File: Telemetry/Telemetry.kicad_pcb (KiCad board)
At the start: 2 copper layers, 56.5 x 55 mm, 61 parts, among them J1 Micro_SD_Card, J5 Conn_02x05_Odd_Even, J7 4P4C, J8 4P4C, Q3 Q_NMOS_GSD, SW1 SW_Push, SW3 SW_Push, U3 MAX485E, U4 STM32F103C8Tx, U5 LD1117S50TR_SOT223, U6 MCP1700-3302E_SOT23, Y1 8Mhz

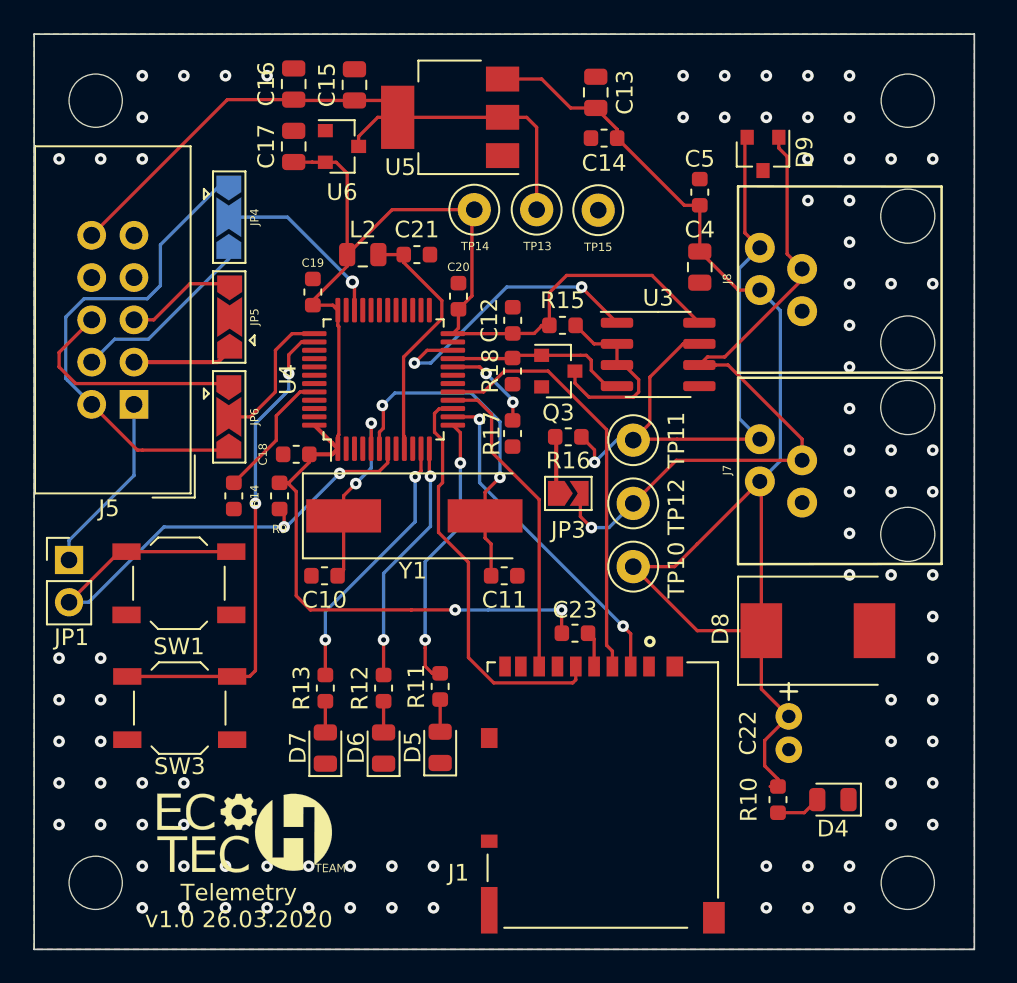
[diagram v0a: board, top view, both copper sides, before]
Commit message: Telemetry/: Gerber fixes
Signed-off-by: Cezarus27 <cs.pol234@gmail.com>
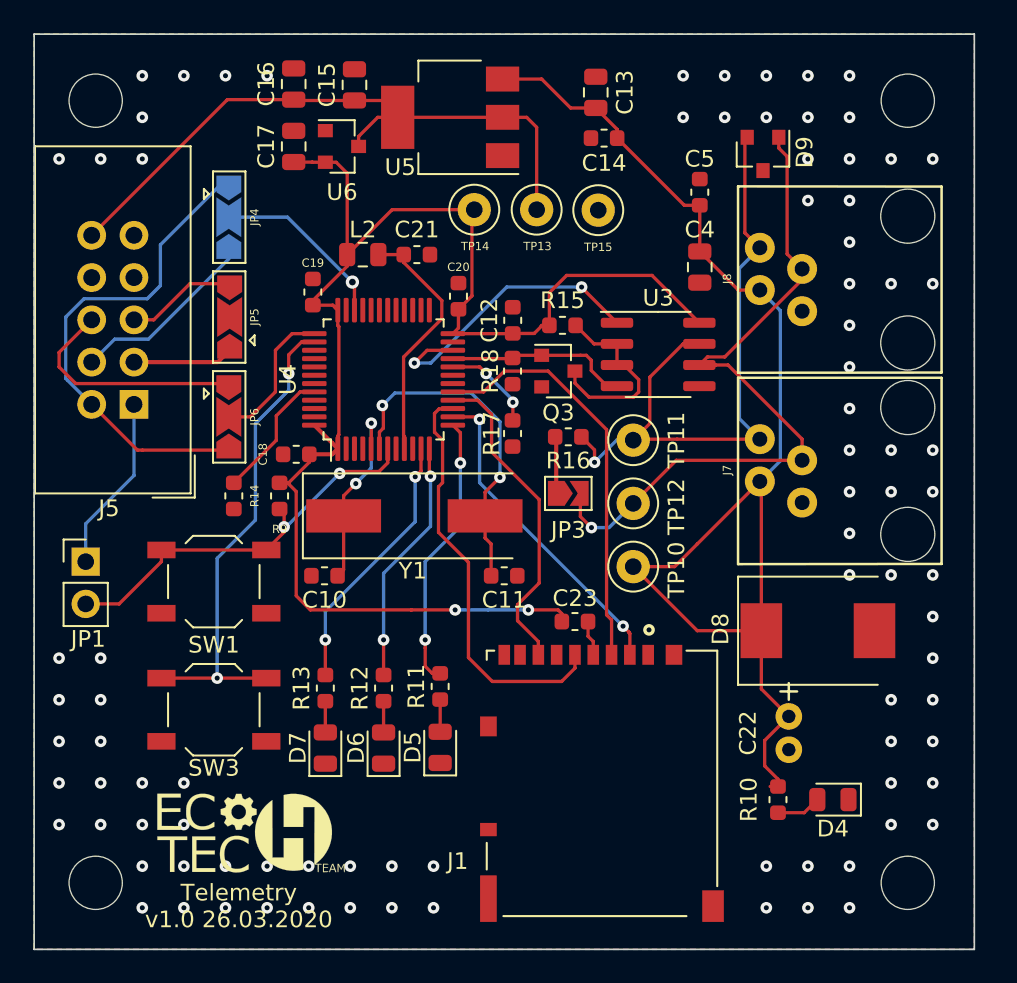
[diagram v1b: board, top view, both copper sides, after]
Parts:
- moved SW1 2.10 mm to (114.3, 132.9)
- moved SW3 2.05 mm to (114.3, 140.6)
- moved JP1 1.00 mm to (106.6, 131.7)
- moved J1 0.70 mm to (137.2, 137.3)
- moved C23 0.70 mm to (136.0, 135.3)
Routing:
- net /RST: track 35.7 -> 24.3 mm
- net +3V3: track 89.2 -> 88.4 mm
- net /MOSI: track 25.6 -> 24.9 mm
- net /CS: track 20.3 -> 19.6 mm

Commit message: Telemetry/: fix PCB size
Signed-off-by: Cezarus27 <cs.pol234@gmail.com>
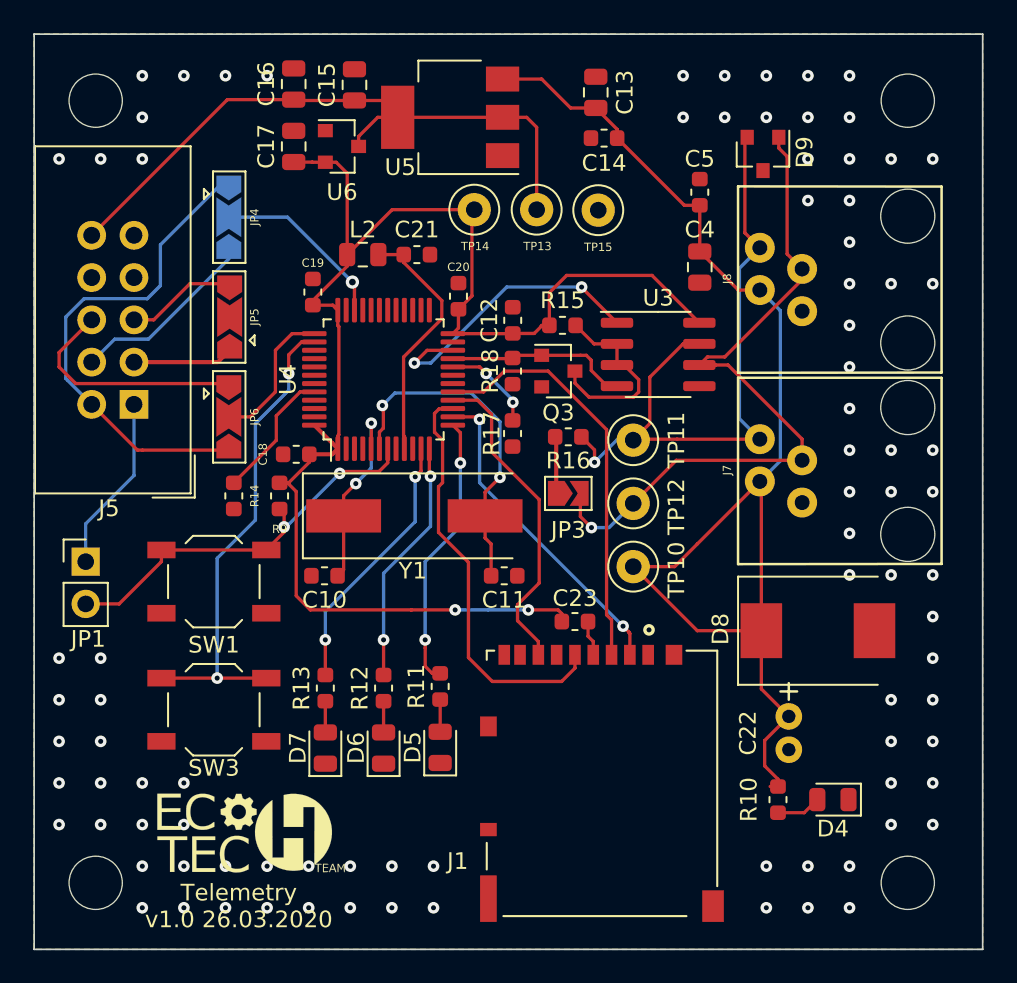
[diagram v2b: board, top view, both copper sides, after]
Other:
- board size 56.5 x 55 mm -> 57 x 55 mm

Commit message: Telemetry/: add test points and rename PCB to v1.3
Signed-off-by: Cezarus27 <cs.pol234@gmail.com>
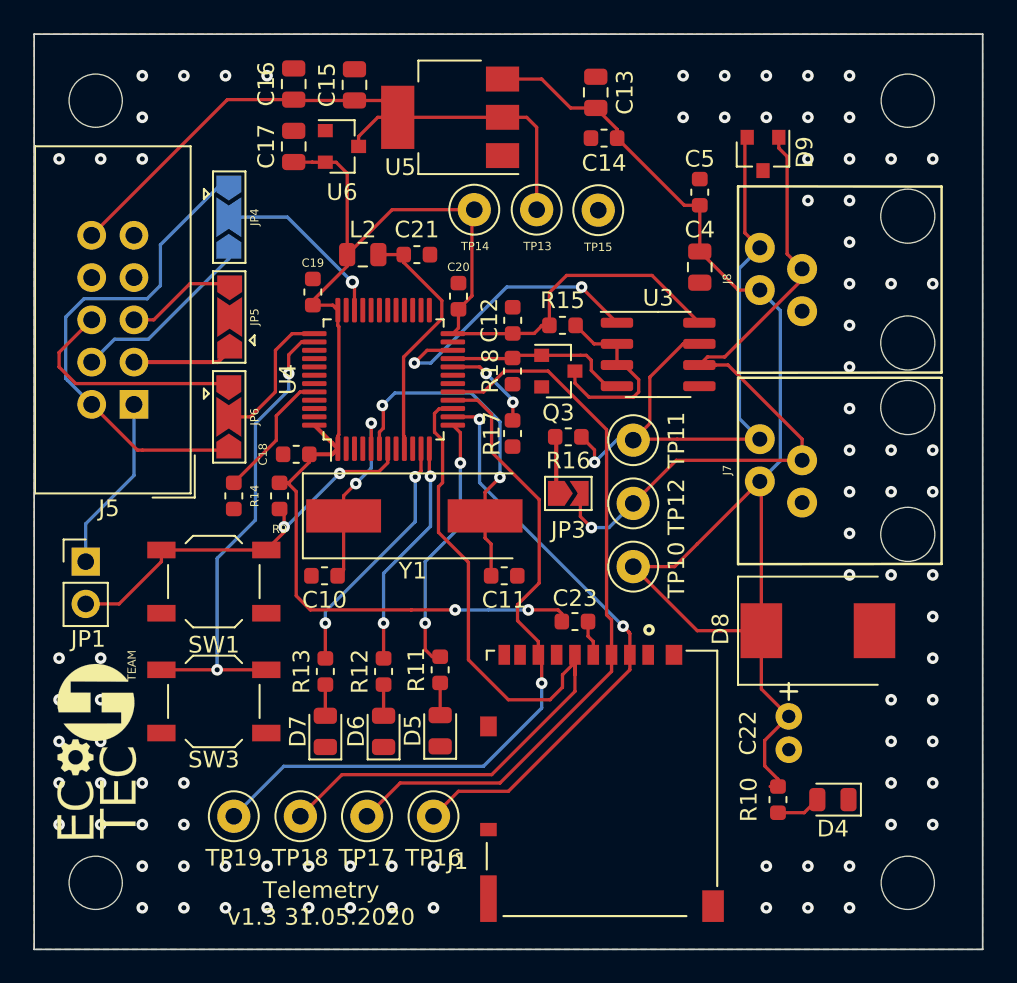
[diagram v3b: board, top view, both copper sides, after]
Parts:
- added TP16: TestPoint, TestPoint:TestPoint_Loop_D1.80mm_Drill1.0mm_Beaded, F.Cu at (127.5, 147.0)
- added TP17: TestPoint, TestPoint:TestPoint_Loop_D1.80mm_Drill1.0mm_Beaded, F.Cu at (123.5, 147.0)
- added TP18: TestPoint, TestPoint:TestPoint_Loop_D1.80mm_Drill1.0mm_Beaded, F.Cu at (119.5, 147.0)
- added TP19: TestPoint, TestPoint:TestPoint_Loop_D1.80mm_Drill1.0mm_Beaded, F.Cu at (115.5, 147.0)
- moved G1 10.2 mm to (107.5, 143.0), turned to 90 degrees
- moved D5 1.00 mm to (127.9, 141.9)
- moved D6 1.00 mm to (124.5, 141.9)
- moved D7 1.00 mm to (121.0, 141.9)
- moved R11 1.00 mm to (127.9, 138.2)
- moved R12 1.00 mm to (124.5, 138.3)
- moved R13 1.00 mm to (121.0, 138.3)
- moved SW3 0.50 mm to (114.3, 140.1)
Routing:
- net /SCK: track 25.1 -> 50.1 mm
- net /MISO: track 19.4 -> 43.8 mm, vias 0 -> 1
- net /MOSI: track 24.9 -> 44.2 mm
- net /CS: track 19.6 -> 35.9 mm
- net /LED3: track 16.3 -> 15.3 mm
- net /LED2: track 14.8 -> 13.8 mm
- net /LED1: track 16.7 -> 15.7 mm
- net Net-(SW3-Pad1): track 29.4 -> 28.9 mm
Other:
- board text added: "Telemetry v1.3 31.05.2020"
- board text removed: "Telemetry v1.0 26.03.2020"

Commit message: Telemetry: bump version to 1.4
- fix ground at PCB
- change track width for 12V
- change jumpers layout
- change font size at fsilks layers

Signed-off-by: Cezary Sobczak <cs.pol234@gmail.com>
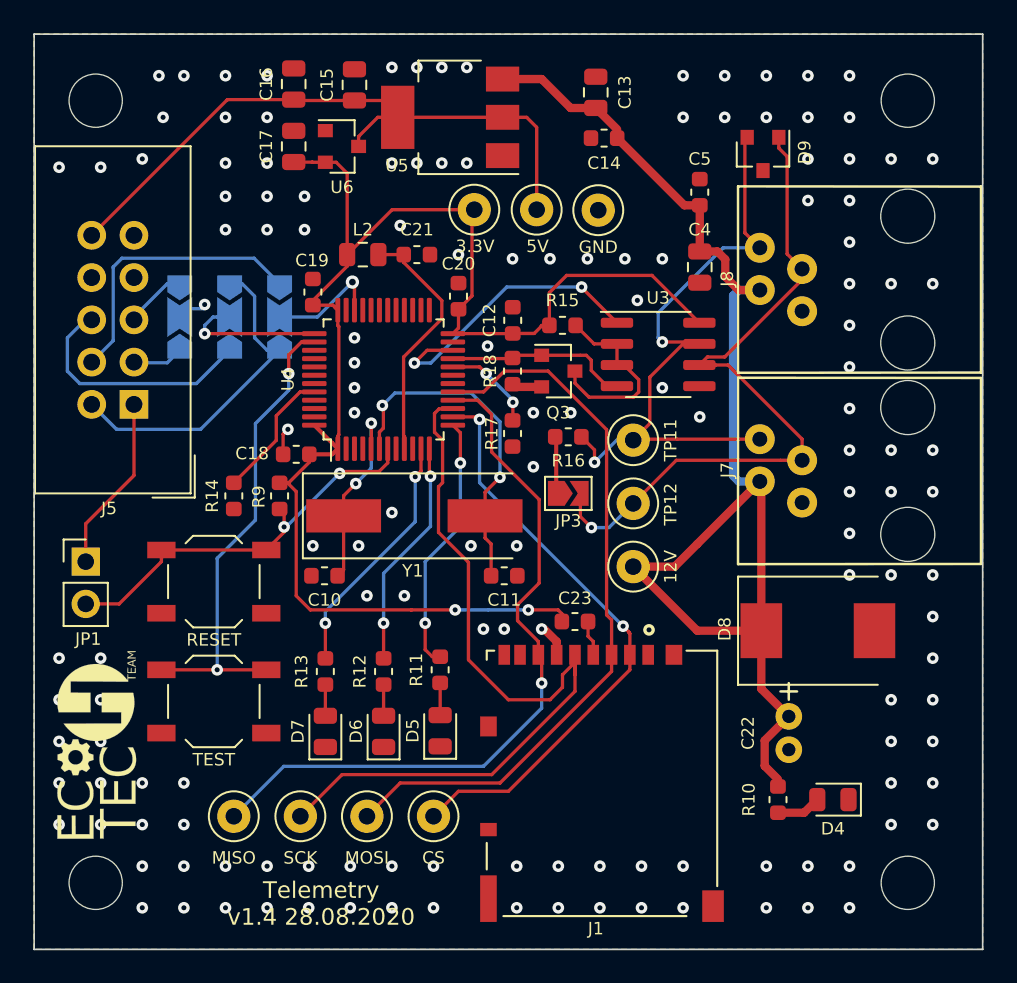
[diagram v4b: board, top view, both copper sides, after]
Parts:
- moved JP4 6.73 mm to (118.2, 117.0), turned to 90 degrees
- moved JP6 6.00 mm to (115.2, 117.0), turned to 90 degrees
- moved JP5 3.00 mm to (112.2, 117.0)
- renumbered TP10 to 12V, TP14 to 3.3V, TP13 to 5V, TP16 to CS, TP15 to GND, TP19 to MISO, TP17 to MOSI, SW1 to RESET, TP18 to SCK, SW3 to TEST
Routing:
- net /2: track 29.8 -> 20.0 mm
- net GND: track 0.00 -> 7.15 mm, vias 87 -> 145
- net /4: track 11.5 -> 17.1 mm
- net /SWDIO: track 10.8 -> 6.98 mm
- net Net-(J5-Pad3): track 6.04 -> 3.08 mm
- net +12V: track 75.8 -> 78.3 mm
- net Net-(J5-Pad5): track 6.65 -> 4.33 mm
- net /B: track 40.4 -> 39.8 mm, vias 1 -> 2
- net /6: track 14.3 -> 14.8 mm
- net /SWCLK: track 8.67 -> 9.15 mm, vias 0 -> 1
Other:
- net class 12V added: clearance 0.2, trace_width 0.5, via_dia 0.7, via_drill 0.3
- rule pad_to_mask_clearance: 0.051 -> 0.1
- rule solder_mask_min_width: 0.25 -> 0.2
- board text added: "STM-LINK"
- board text added: "Telemetry v1.4 28.08.2020"
- board text removed: "Telemetry v1.3 31.05.2020"
